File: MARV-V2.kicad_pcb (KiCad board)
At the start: 4 copper layers, 48.7 x 41.2 mm, 140 parts, among them J10 DBG pads (SWCLK SWDIO GND), J11 microSD, Molex 104031-0811 pu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, J3 ESC pads (CURR TX M4 M3 M2 M1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, J4 USB_C_PROGRAM_POWER, J6 IO array signal column (inner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, J7 IO array power column (5V / 3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, J8 IO array GND column (board ed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, SW1 RESET (RUN to GND), SW2 BOOTSEL (via R24), U12 TPS7A2033PDBVR, U20 RP2354B, U21 ICM-45686 6-axis IMU, U22 BMP581 barometer, U23 ADXL375 high-g accelerometer, U24 W25Q64JVSSIQ, 64 Mbit QSPI NOR, U25 TPS2121RUXR, U26 AP63205WU-7, U7 TPS62913RPUR, U8 USBLC6-2SC6, Y1 12 MHz ABM8-272-T3, CL 10 pF

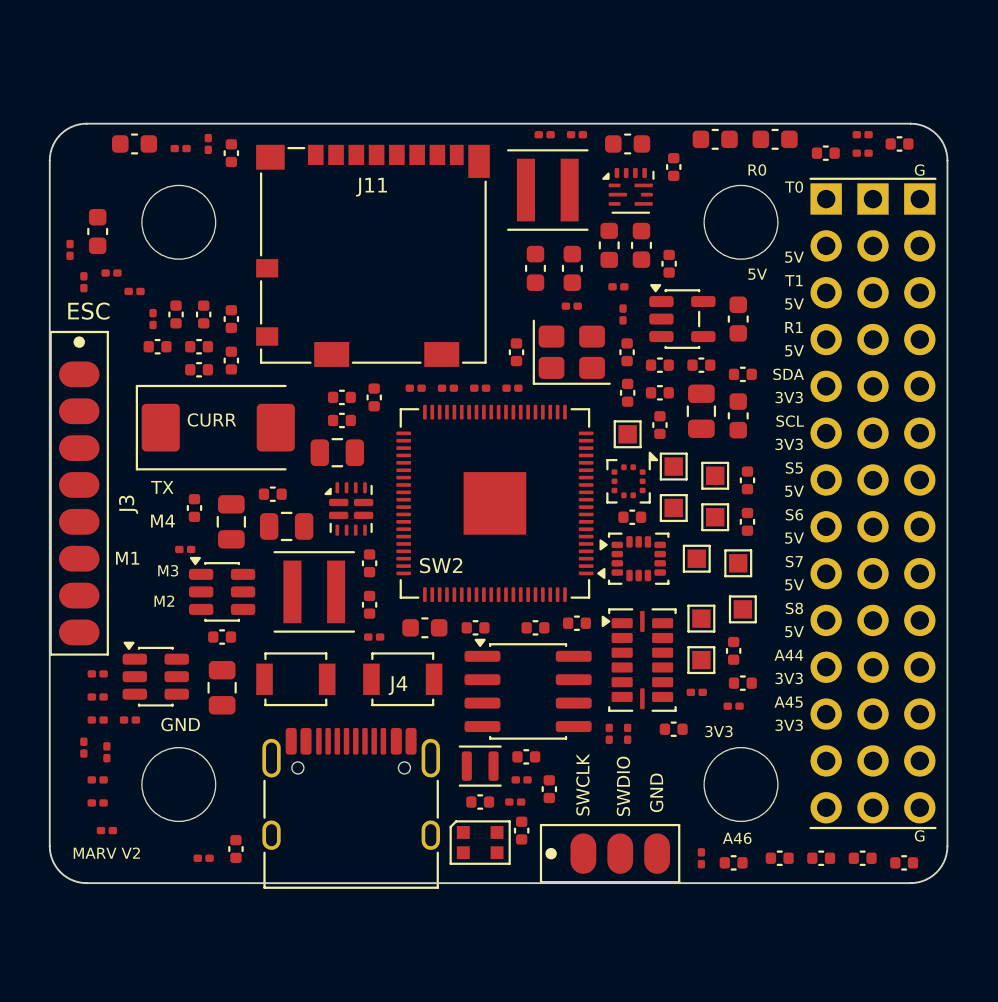
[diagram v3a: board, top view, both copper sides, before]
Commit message: ESC row, DBG pads and test points to the back; board 46.6 x 41.2 mm; fixed IO-block silk
The ESC pad row J3, the DBG pad row J10 and TP1-TP10 are placed flipped on
B.Cu (bare pads only; assembly stays single-sided on the front). The back
faces the ESC in the stack, so the 8-wire harness runs straight down; the
labels are mirrored B.SilkS text in bands nothing else can reach. With the
left margin freed, the left holes sit 4.0 mm from the edge and the board
shrinks to 46.6 x 41.2 mm (39-40 mm heights fail the packer). The IO-block
labels on the front are now fixed in a reserved band instead of being
nudged, so no silk collides. DRC: unrouted items only, front and back.
ERC 0/0, checker PASS (140 components), ngspice PASS, audit 140/140.

Co-Authored-By: Claude Fable 5.1 <noreply@anthropic.com>
Claude-Session: https://claude.ai/code/session_01U6Ud7JA3CDTJZVcZZr5sx1
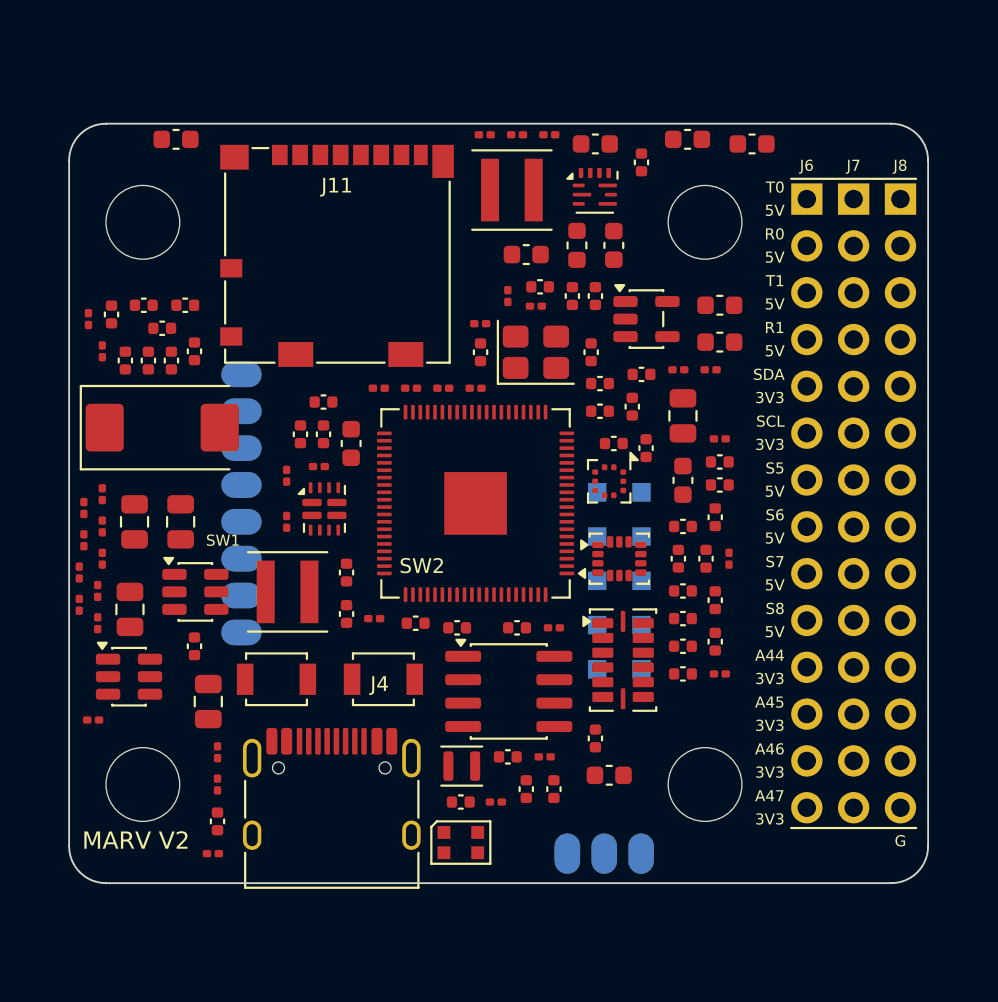
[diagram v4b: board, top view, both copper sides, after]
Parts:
- J10, J3, TP1, TP10, TP2, TP3, TP4, TP5, TP6, TP7, TP8, TP9: moved to B.Cu
- moved C20 42.9 mm to (106.0, 114.8)
- moved R26 31.2 mm to (111.5, 92.8)
- moved C61 29.3 mm to (110.0, 109.2)
- moved C45 28.5 mm to (105.2, 112.8)
- moved R25 28.3 mm to (109.8, 92.8), turned to 0 degrees
- moved C43 25.3 mm to (83.5, 91.8), turned to 90 degrees
- moved C60 23.9 mm to (112.0, 97.8)
- moved R41 23.2 mm to (99.0, 90.2)
- moved C64 22.1 mm to (89.2, 96.2), turned to 90 degrees
- moved R10 21.1 mm to (100.5, 88.8), turned to 90 degrees
- moved C57 21.0 mm to (112.0, 99.0)
- moved C26 20.1 mm to (104.0, 88.8)
- moved C25 18.4 mm to (105.2, 88.8), turned to 90 degrees
- moved R40 18.4 mm to (90.2, 98.0), turned to 0 degrees
- moved R51 17.3 mm to (112.0, 96.5)
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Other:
- board size 48.7 x 41.2 mm -> 46.6 x 41.2 mm
- board text added: "A47"
- board text added: "VBAT"

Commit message: Flash socket becomes an optional back-side expansion; ESC row on the back edge; C19 100 uF
U24 (SOIC-8 150 mil) and its caps C62/C63 are DNP, excluded from the BOM
and placed flipped on the back with a legend ("FLASH / PSRAM EXPANSION,
SOIC-8 150mil, QMI CS1, W25Q64JVSSIQ or APS6404L-3SQR-SN"); the RP2354B's
internal 2 MB flash and the microSD cover firmware and logging. The ESC pad
row J3 sits along the left edge on the back, like the DBG row on the bottom
edge. C19 (V5_SYS bulk) reduced from 220 uF D-case to 100 uF 6.3 V B-case:
the ngspice decks now use CPOLY=100u and every handover predicate still
passes (worst-case V5_SYS min 4.37 V). Board 46.6 x 41.2 mm; DRC
unrouted-only; ERC 0/0, checker PASS, audit 140/140.

Co-Authored-By: Claude Fable 5.1 <noreply@anthropic.com>
Claude-Session: https://claude.ai/code/session_01U6Ud7JA3CDTJZVcZZr5sx1
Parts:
- C19: value 220u / 10 V polymer, ESR ~40 mOhm -> 100u / 6.3 V polymer, ESR <= 40 mOhm (e.g. Panasonic 6TPE100MAZB or KEMET T520/T530 B case); footprint Capacitor_Tantalum_SMD:CP_EIA-7343-31_Kemet-D -> Capacitor_Tantalum_SMD:CP_EIA-3528-21_Kemet-B
- C62: value 100n / 16 V X7R, U24 VCC -> DNP: 100n / 16 V X7R, U24 VCC; moved to B.Cu
- C63: value 1u / 10 V X7R 0402, U24 VCC -> DNP: 1u / 10 V X7R 0402, U24 VCC; moved to B.Cu
- U24: value W25Q64JVSSIQ, 64 Mbit QSPI NOR -> DNP: W25Q64JVSSIQ, 64 Mbit QSPI NOR (optional back-side expansion); moved to B.Cu
- moved C21 40.2 mm to (106.5, 112.5)
- moved C20 24.3 mm to (112.0, 91.2)
- moved C65 21.7 mm to (88.8, 94.2), turned to 0 degrees
- moved C41 20.9 mm to (86.5, 98.2)
- moved C40 18.8 mm to (92.2, 106.0)
- moved C42 16.6 mm to (103.5, 109.0), turned to 90 degrees
- moved R40 16.4 mm to (104.0, 89.0), turned to 90 degrees
- moved C39 14.1 mm to (105.2, 96.2), turned to 90 degrees
- moved R10 13.8 mm to (112.5, 95.5)
- moved R41 12.3 mm to (88.2, 96.2), turned to 90 degrees
- moved R29 12.2 mm to (87.2, 96.8)
- moved R43 11.9 mm to (81.0, 89.2), turned to 0 degrees
- moved C64 11.9 mm to (99.0, 89.5)
- moved R45 11.8 mm to (78.5, 89.5)
- moved C80 11.3 mm to (83.2, 99.5), turned to 0 degrees
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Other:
- board text added: "1"
- board text added: "APS6404L-3SQR-SN"
- board text added: "FLASH / PSRAM EXPANSION"
- board text added: "SOIC-8 150mil, QMI CS1"
- board text added: "W25Q64JVSSIQ or"

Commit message: Flash-socket caps back on the front, minimal socket silk; L2 to XGL3020-222
C62/C63 (U24 decoupling) are fitted on the front again, so a user adding a
flash or PSRAM chip to the back-side SOIC-8 socket only solders the chip;
the back legend is reduced to "FLASH" / "SOIC-8" plus the pin-1 mark, and
the compatible parts (150-mil SOIC-8 QSPI NOR: W25Q16/32/64JVSS, GD25Q32C/
64C, MX25L3233F/6433F; QSPI PSRAM: APS6404L-3SQR-SN, ESP-PSRAM64H, IPS6404L,
LY68L6400) are documented in DESIGN_SPEC/LIBRARIES.

L2 (TPS62913 3.3 V buck inductor) shrinks from XGL4030-222 (4x4x3.1) to
Coilcraft XGL3020-222MEC (3x3x2.0; Isat 2.2 A @20 %, 2.85 A @30 %, DCR
30.5 mOhm, Doc 1776 Rev 02/19/26) against a ~0.95 A peak; project footprint
from the Coilcraft land pattern, vendor STEP aligned and verified against
copper. L3 stays XGL4030-472: its floor is the AP63205's 3.1 A current-limit
ceiling and the XGL4020 shares the 4x4 land pattern. Board 46.6 x 41.2 mm;
DRC unrouted-only; ERC 0/0, checker PASS, ngspice PASS, audit 140/140.

Co-Authored-By: Claude Fable 5.1 <noreply@anthropic.com>
Claude-Session: https://claude.ai/code/session_01U6Ud7JA3CDTJZVcZZr5sx1
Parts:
- C62: value DNP: 100n / 16 V X7R, U24 VCC -> 100n / 16 V X7R, U24 VCC (fitted; socket is optional); moved to F.Cu
- C63: value DNP: 1u / 10 V X7R 0402, U24 VCC -> 1u / 10 V X7R 0402, U24 VCC (fitted; socket is optional); moved to F.Cu
- L2: value 2.2u / Isat 7 A, DCR 13.5 mOhm (Coilcraft XGL4030-222MEC or equiv) -> 2.2u / Isat 2.2 A (20 %), DCR 30.5 mOhm (Coilcraft XGL3020-222MEC); footprint MARV_Packages:L_Coilcraft_XxL4030 -> MARV_Packages:L_Coilcraft_XGL3020
- moved C21 32.8 mm to (113.8, 80.5)
- moved R9 10.6 mm to (107.2, 87.0), turned to 90 degrees
- moved C12 10.4 mm to (103.0, 87.8)
- moved R7 6.91 mm to (107.2, 85.2), turned to 90 degrees
- moved C11 6.25 mm to (101.8, 80.2)
- moved C9 3.51 mm to (110.2, 80.2)
- moved C13 3.40 mm to (100.2, 85.5)
- moved R8 1.82 mm to (99.2, 80.5)
- moved FB1 1.27 mm to (103.0, 85.8), turned to 0 degrees
- moved C10 0.50 mm to (105.8, 86.0)
- moved R40 0.35 mm to (103.8, 89.2), turned to 0 degrees
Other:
- board text added: "FLASH"
- board text added: "SOIC-8"
- board text removed: "APS6404L-3SQR-SN"
- board text removed: "FLASH / PSRAM EXPANSION"
- board text removed: "SOIC-8 150mil, QMI CS1"
- board text removed: "W25Q64JVSSIQ or"

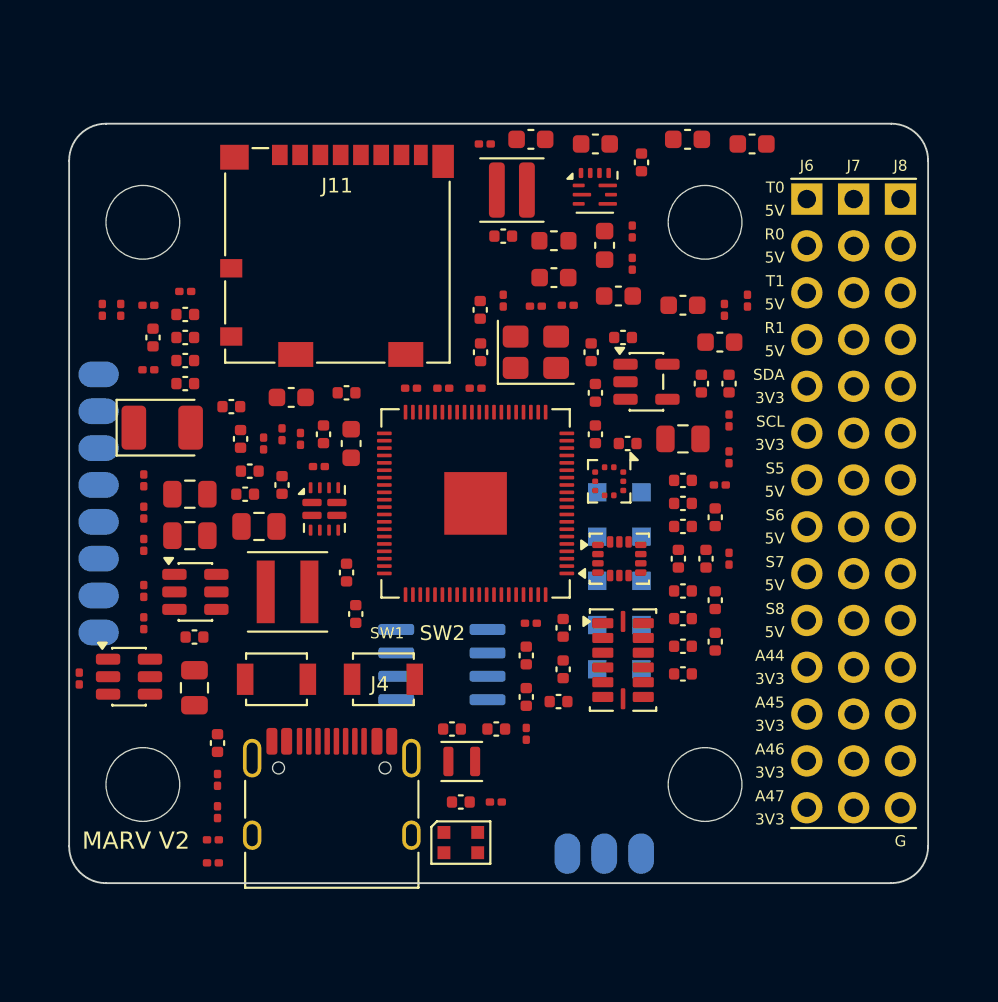
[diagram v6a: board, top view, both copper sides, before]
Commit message: JLCPCB sourcing: Basic-part refactor, LCSC numbers in the schematic, order files and audit
Parts audited line by line against JLCPCB's live catalogue (tools/jlc/,
reports/jlc-audit.md). Resistors move 0201 -> 0402 (JLC's Basic library has
no 0201 resistor), the U7 FB divider becomes 10k/3.16k 0.1 % (15.8k 0.1 % is
not stocked), Y1 becomes TAXM12M4RFBCCT2T (CL 12 pF) with 18 pF loads, L2/L3
become CJIANG FTC303020D2R2MBCA / FTC404030S4R7MGCA (stocked; Isat 5.5 A /
6.0 A at 30 %, footprints + models vendored from KiCad), the 22 uF/25 V and
10 uF lines move to Basic parts. The U24 default fit is W25Q32JVSNIQ (the
W25Q64JVSSIQ is a 208-mil part and never fitted the 150-mil socket).

Every fitted symbol carries a hidden LCSC property stamped from
tools/jlc/lcsc_map.csv; tools/jlc/export_jlc.py writes reports/jlc-bom.csv
and reports/jlc-cpl.csv (top-side SMT, headers unpopulated, U24 DNP).
Result: 46 unique parts, 16 Basic / 1 Preferred / 29 Extended (was 9/1/35),
extended-fee estimate $87 (was $105), $45.68 per board at 10 (was $52.97 with
L2 unsourced). DESIGN_SPEC gains a Manufacturing (JLCPCB) section with the
quote parameters. Board rebuilt (0 fit/geometry, DRC unrouted-only); ERC
0/0, checker PASS, ngspice PASS, audit 140/140.

Co-Authored-By: Claude Fable 5.1 <noreply@anthropic.com>
Claude-Session: https://claude.ai/code/session_01U6Ud7JA3CDTJZVcZZr5sx1
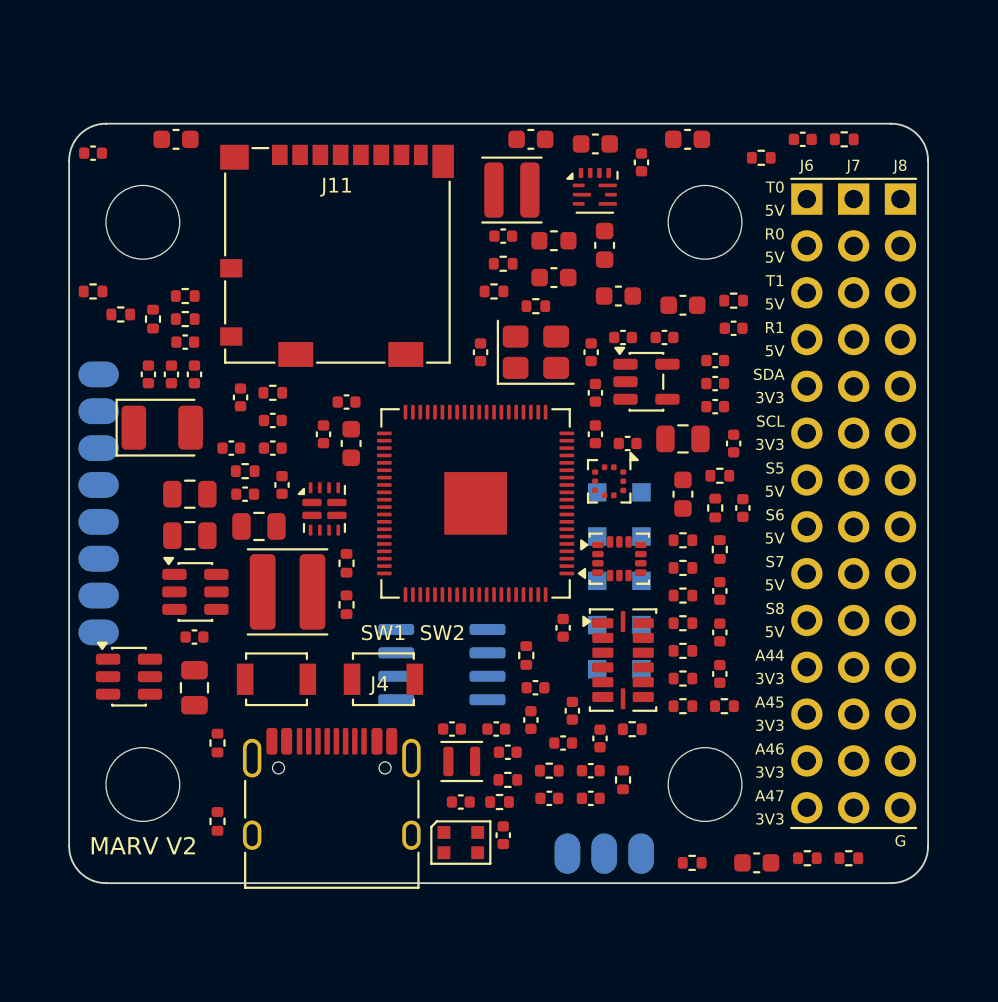
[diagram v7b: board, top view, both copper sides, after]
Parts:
- C46, C47: value 15p / 50 V C0G -> 18p / 50 V C0G
- L2: value 2.2u / Isat 2.2 A (20 %), DCR 30.5 mOhm (Coilcraft XGL3020-222MEC) -> 2.2u / Isat 5.5 A (30 %), DCR 45 mOhm max (CJIANG FTC303020D2R2MBCA); footprint MARV_Packages:L_Coilcraft_XGL3020 -> MARV_Packages:L_Changjiang_FTC303020D
- L3: value 4.7u, Isat 4.4 A, DCR 31.5 mOhm max (Coilcraft XGL4030-472MEC) -> 4.7u, Isat 6.0 A (30 %), DCR 46 mOhm max (CJIANG FTC404030S4R7MGCA); footprint MARV_Packages:L_Coilcraft_XxL4030 -> MARV_Packages:L_Changjiang_FTC404030S
- R10, R20, R21, R22, R23, R24, R25, R26, R27, R28, R29, R30, R35, R36, R37, R38, R39, R4, R40, R41, R42, R43, R44, R45, R46, R47, R48, R5, R50, R51, R52, R53, R54, R55, R9: footprint Resistor_SMD:R_0201_0603Metric -> Resistor_SMD:R_0402_1005Metric
- R7: value 15.8k / 0.1% -> 10k / 0.1%; footprint Resistor_SMD:R_0201_0603Metric -> Resistor_SMD:R_0402_1005Metric
- R8: value 4.99k / 0.1% -> 3.16k / 0.1%; footprint Resistor_SMD:R_0201_0603Metric -> Resistor_SMD:R_0402_1005Metric
- U24: value DNP: W25Q64JVSSIQ, 64 Mbit QSPI NOR (optional back-side expansion) -> DNP: W25Q32JVSNIQ, 32 Mbit QSPI NOR or APS6404L-SQN-SN 8 MB PSRAM (optional back-side expansion)
- Y1: value 12 MHz ABM8-272-T3, CL 10 pF -> 12 MHz TAXM12M4RFBCCT2T, CL 12 pF
- moved R30 50.8 mm to (118.8, 80.2), turned to 0 degrees
- moved R54 47.3 mm to (119.0, 119.2)
- moved C21 39.0 mm to (114.0, 119.5)
- moved R29 37.1 mm to (116.8, 119.2), turned to 0 degrees
- moved R28 32.5 mm to (110.5, 119.5), turned to 0 degrees
- moved C20 31.5 mm to (82.5, 80.2)
- moved R27 29.0 mm to (106.8, 115.0)
- moved R4 26.5 mm to (110.0, 111.0)
- moved R41 25.5 mm to (110.0, 109.5), turned to 0 degrees
- moved R26 24.1 mm to (107.2, 112.2), turned to 0 degrees
- moved C65 21.9 mm to (110.0, 99.5), turned to 90 degrees
- moved R25 21.5 mm to (112.2, 111.0), turned to 0 degrees
- moved C41 20.7 mm to (100.5, 113.5)
- moved R39 20.0 mm to (110.0, 106.5), turned to 0 degrees
- moved R40 19.8 mm to (110.0, 108.0)
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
